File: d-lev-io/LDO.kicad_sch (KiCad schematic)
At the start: 7 parts, among them U1 AP1117-ADJ

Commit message: many many changes'
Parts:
- removed R13: 3920, Resistor_SMD:R_0805_2012Metric_Pad1.20x1.40mm_HandSolder, symbol Device:R_Small
- removed R14: 10k, Resistor_SMD:R_0805_2012Metric_Pad1.20x1.40mm_HandSolder, symbol Device:R_Small
- removed U1: AP1117-ADJ, Package_TO_SOT_SMD:SOT-223-3_TabPin2, symbol Regulator_Linear:AP1117-ADJ
- added C2: 10u, symbol Device:C_Small
- added U5: MIC5219-3.3YM5, Package_TO_SOT_SMD:SOT-23-5, symbol Regulator_Linear:MIC5219-3.3YM5
- C2: value 1u -> 10u
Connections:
- net GND: now also C2.1, U5.2 (GND)
- net VIN: now also U5.1 (IN), U5.3 (EN)
- net VOUT: now also C2.2, U5.5 (OUT)
- no-connect marks 0 -> 1
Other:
- moved on the sheet: C2

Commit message: many more changes
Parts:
- removed C2 (x2): .1u, symbol Device:C_Small
- removed C2: 1u, symbol Device:C_Small
- removed C2: 10u, symbol Device:C_Small
- added C2 (x2): .1u, Capacitor_SMD:C_0603_1608Metric, symbol Device:C_Small
- added C2: 1u, Capacitor_SMD:C_0603_1608Metric, symbol Device:C_Small
- added C2: 10u, Capacitor_SMD:C_0805_2012Metric, symbol Device:C_Small
- C2: footprint (none) -> Capacitor_SMD:C_0805_2012Metric
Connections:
- net GND: now also C2.1, C2.1, C2.1, C2.1
- net VIN: now also C2.2, C2.2
- net VOUT: now also C2.2, C2.2

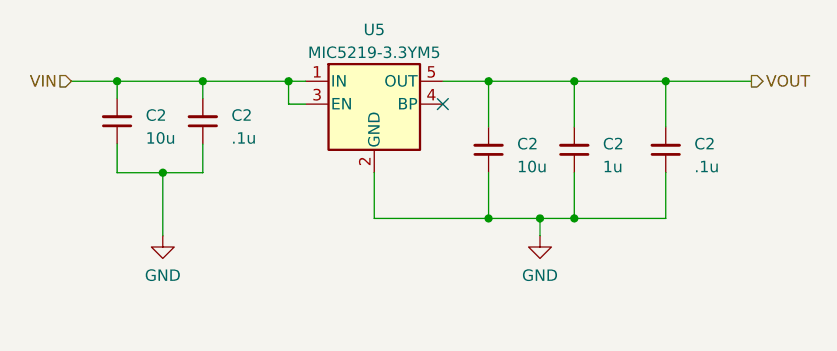
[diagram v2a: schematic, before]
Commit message: map SAMD21 pins
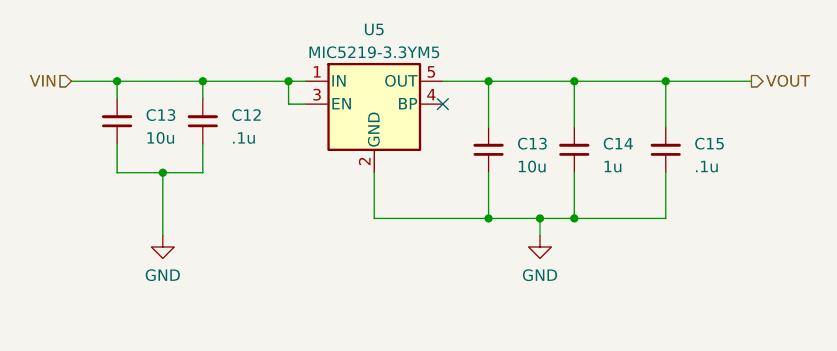
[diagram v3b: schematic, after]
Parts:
- renumbered C2 to C12, C2 to C13, C2 to C14, C2 to C15
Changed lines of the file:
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@@
   (symbol (lib_id "Device:C_Small") (at 99.06 88.265 180) (unit 1)
     (in_bom yes) (on_board yes) (dnp no) (fields_autoplaced)
-    (property "Reference" "C2" (at 102.235 87.6236 0)
+    (property "Reference" "C12" (at 102.235 87.6236 0)
       (effects (font (size 1.27 1.27)) (justify right))
     )
@@
     (instances
       (project "d-lev-io"
-        (path "/9261a07b-ae4a-4d72-8042-ea097cd0e5ed/2e03420b-b293-43b9-bc55-2ad53210d7d7"
-          (reference "C2") (unit 1)
-        )
         (path "/9261a07b-ae4a-4d72-8042-ea097cd0e5ed"
           (reference "C12") (unit 1)
@@
   (symbol (lib_id "Device:C_Small") (at 150.495 91.44 180) (unit 1)
     (in_bom yes) (on_board yes) (dnp no) (fields_autoplaced)
-    (property "Reference" "C2" (at 153.67 90.7986 0)
+    (property "Reference" "C15" (at 153.67 90.7986 0)
       (effects (font (size 1.27 1.27)) (justify right))
     )
@@
     (instances
       (project "d-lev-io"
-        (path "/9261a07b-ae4a-4d72-8042-ea097cd0e5ed/2e03420b-b293-43b9-bc55-2ad53210d7d7"
-          (reference "C2") (unit 1)
-        )
         (path "/9261a07b-ae4a-4d72-8042-ea097cd0e5ed"
           (reference "C15") (unit 1)
@@
   (symbol (lib_id "Device:C_Small") (at 140.335 91.44 180) (unit 1)
     (in_bom yes) (on_board yes) (dnp no) (fields_autoplaced)
-    (property "Reference" "C2" (at 143.51 90.7986 0)
+    (property "Reference" "C14" (at 143.51 90.7986 0)
       (effects (font (size 1.27 1.27)) (justify right))
     )
@@
     (instances
       (project "d-lev-io"
-        (path "/9261a07b-ae4a-4d72-8042-ea097cd0e5ed/2e03420b-b293-43b9-bc55-2ad53210d7d7"
-          (reference "C2") (unit 1)
-        )
         (path "/9261a07b-ae4a-4d72-8042-ea097cd0e5ed"
           (reference "C14") (unit 1)
@@
   (symbol (lib_id "Device:C_Small") (at 89.535 88.265 180) (unit 1)
     (in_bom yes) (on_board yes) (dnp no) (fields_autoplaced)
-    (property "Reference" "C2" (at 92.71 87.6236 0)
+    (property "Reference" "C13" (at 92.71 87.6236 0)
       (effects (font (size 1.27 1.27)) (justify right))
     )
@@
     (instances
       (project "d-lev-io"
-        (path "/9261a07b-ae4a-4d72-8042-ea097cd0e5ed/2e03420b-b293-43b9-bc55-2ad53210d7d7"
-          (reference "C2") (unit 1)
-        )
         (path "/9261a07b-ae4a-4d72-8042-ea097cd0e5ed"
           (reference "C13") (unit 1)
@@
   (symbol (lib_id "Device:C_Small") (at 130.81 91.44 180) (unit 1)
     (in_bom yes) (on_board yes) (dnp no) (fields_autoplaced)
-    (property "Reference" "C2" (at 133.985 90.7986 0)
+    (property "Reference" "C13" (at 133.985 90.7986 0)
       (effects (font (size 1.27 1.27)) (justify right))
     )
@@
     (instances
       (project "d-lev-io"
-        (path "/9261a07b-ae4a-4d72-8042-ea097cd0e5ed/2e03420b-b293-43b9-bc55-2ad53210d7d7"
-          (reference "C2") (unit 1)
-        )
         (path "/9261a07b-ae4a-4d72-8042-ea097cd0e5ed"
           (reference "C13") (unit 1)

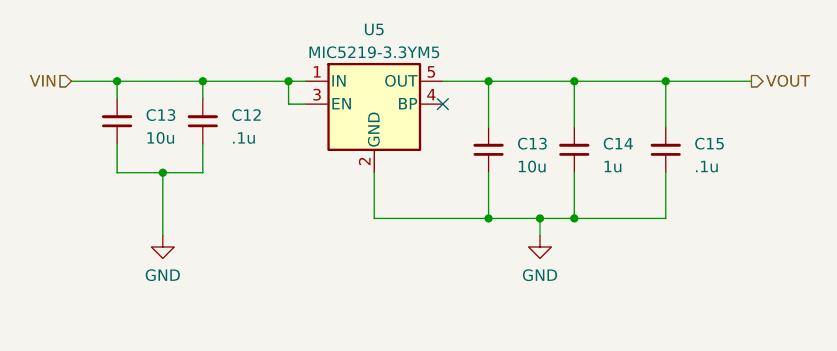
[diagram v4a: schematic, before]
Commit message: io board more analog schematic capture
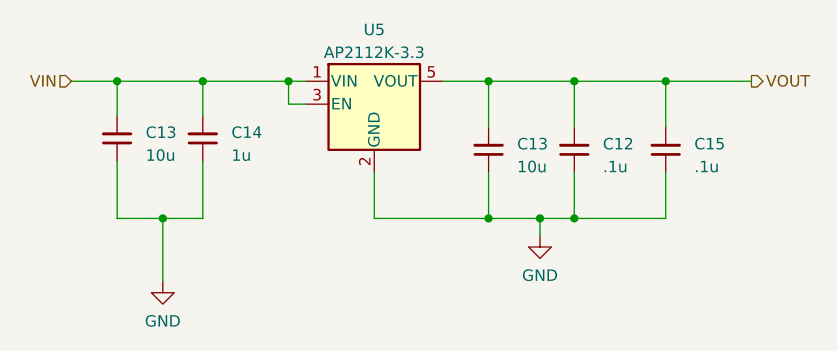
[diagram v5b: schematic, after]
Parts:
- removed U5: MIC5219-3.3YM5, Package_TO_SOT_SMD:SOT-23-5, symbol Regulator_Linear:MIC5219-3.3YM5
- added U5: AP2112K-3.3, Package_TO_SOT_SMD:SOT-23-5, symbol Regulator_Linear:AP2112K-3.3
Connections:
- net GND: now also U5.2 (GND)
- net VIN: now also C14.2, U5.1 (VIN), U5.3 (EN); no longer C12.2
- net VOUT: now also C12.2, U5.5 (VOUT); no longer C14.2
- no-connect marks 1 -> 0
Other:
- moved on the sheet: C12, C13, C14

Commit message: many board updates
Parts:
- C12: value .1u -> 1u
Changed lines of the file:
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@@
       (effects (font (size 1.27 1.27)) (justify right))
     )
-    (property "Value" ".1u" (at 143.51 93.3386 0)
+    (property "Value" "1u" (at 143.51 93.3386 0)
       (effects (font (size 1.27 1.27)) (justify right))
     )
